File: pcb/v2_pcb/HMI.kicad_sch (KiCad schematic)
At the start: 34 parts, among them SW1101 BUTTON 1, SW1102 BUTTON 2, SW1103 BUTTON 3, U1100 SN74AHCT1G125DCKR, U1101 SN74AHCT1G125DCKR

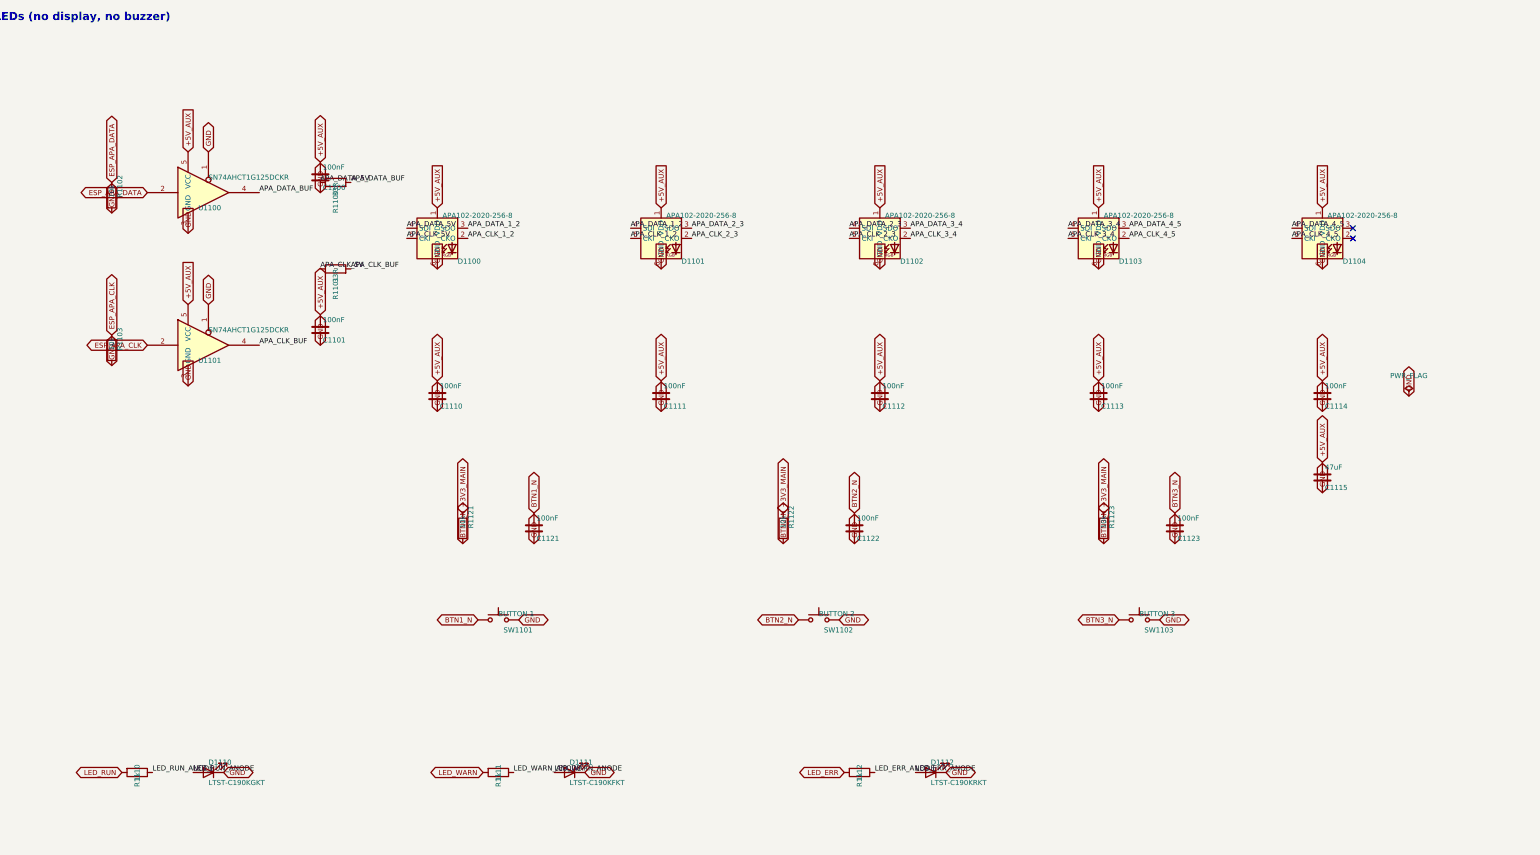
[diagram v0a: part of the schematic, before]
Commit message: switch mosfets
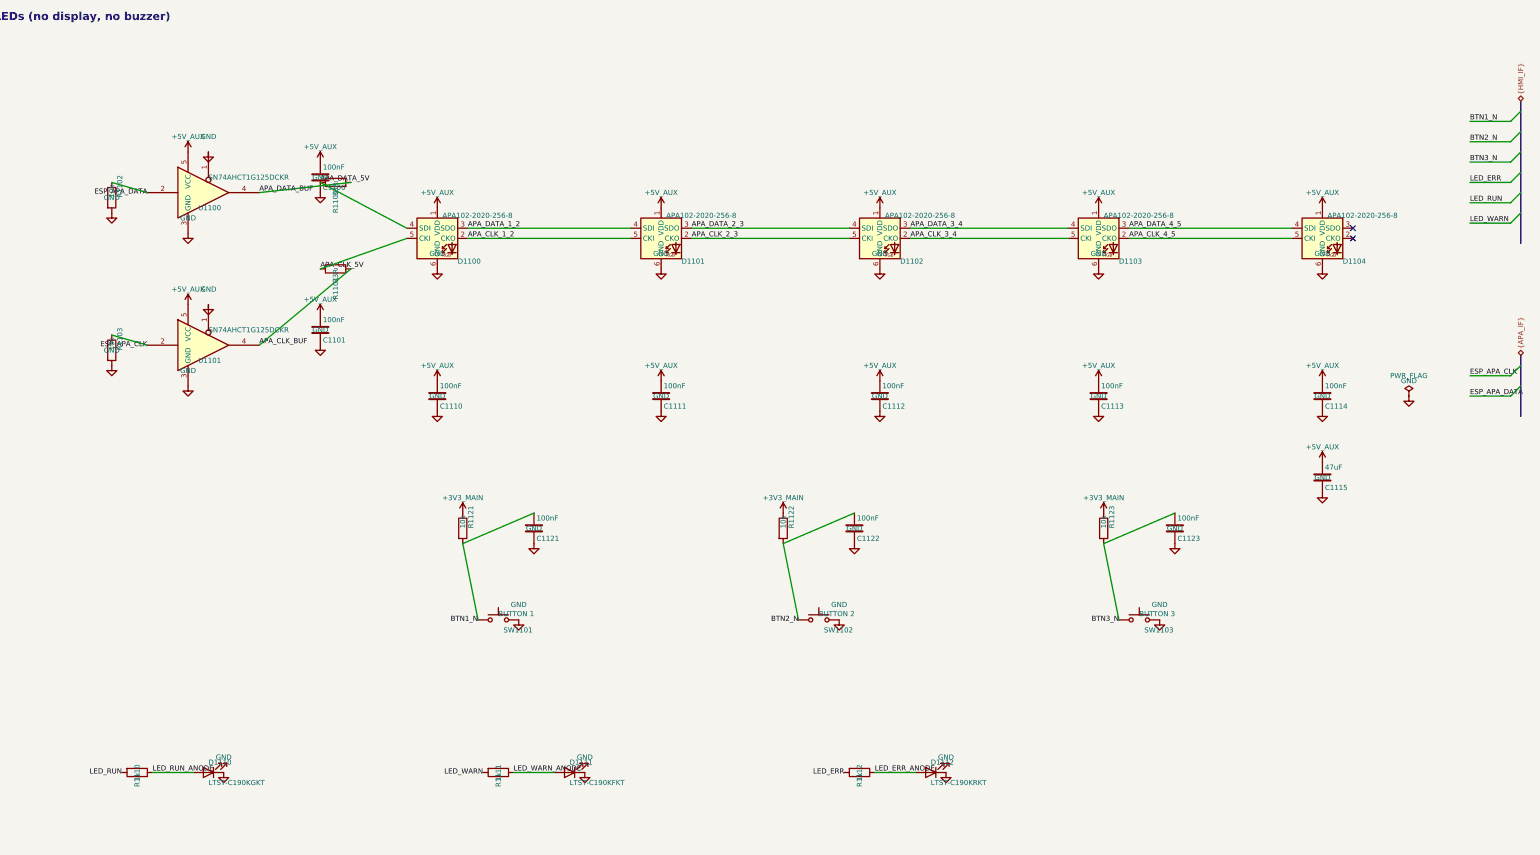
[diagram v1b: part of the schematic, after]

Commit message: minor fixes
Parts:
- C1100, C1101, C1110, C1111, C1112, C1113, C1114, C1121, C1122, C1123: value 100nF -> 100nF 50V X7R; Dielectric (none) -> X7R; MPN (none) -> CGA2B3X7R1H104K050BE; Manufacturer (none) -> TDK; Qualification (none) -> AEC-Q200; Termination (none) -> Soft termination; Tolerance (none) -> ±10%; Voltage (none) -> 50 VDC
- C1115: value 47uF -> 47uF 10V X7R; footprint Capacitor_SMD:C_0805_2012Metric -> Capacitor_SMD:C_1210_3225Metric; Dielectric (none) -> X7R; MPN (none) -> C1210X476K8RACAUTO; Manufacturer (none) -> KEMET (Yageo Group); Qualification (none) -> AEC-Q200; Release_Status (none) -> Verify effective capacitance under worst-case DC bias; Termination (none) -> FT-CAP flexible termination; Tolerance (none) -> ±10%; Voltage (none) -> 10 VDC
- D1100, D1101, D1102, D1103, D1104: Design_Note (none) -> Include the five LEDs in the +5V_AUX worst-case current and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; Manufacturer APA Electronic -> iPixel LED Light Co., Ltd.
- D1110: value LTST-C190KGKT -> ASMT-RF45-AN002 YELLOW GREEN; Color (none) -> Yellow green; Current (none) -> 20 mA maximum; visual-qualify at fitted 1 kΩ drive; MPN LTST-C190KGKT -> ASMT-RF45-AN002; Manufacturer Lite-On -> Broadcom; Operating_Temperature (none) -> -40 to +100 °C; Qualification (none) -> Automotive qualified
- D1111: value LTST-C190KFKT -> ASMT-RJ45-AQ502 ORANGE; Color (none) -> Orange; Current (none) -> 20 mA maximum; visual-qualify at fitted 1 kΩ drive; MPN LTST-C190KFKT -> ASMT-RJ45-AQ502; Manufacturer Lite-On -> Broadcom; Operating_Temperature (none) -> -40 to +100 °C; Qualification (none) -> Automotive qualified
- D1112: value LTST-C190KRKT -> ASMT-RR45-AQ902 RED; Color (none) -> Red; Current (none) -> 20 mA maximum; visual-qualify at fitted 1 kΩ drive; MPN LTST-C190KRKT -> ASMT-RR45-AQ902; Manufacturer Lite-On -> Broadcom; Operating_Temperature (none) -> -40 to +100 °C; Qualification (none) -> Automotive qualified
- R1100, R1101: MPN (none) -> CRCW040233R0FKED; Manufacturer (none) -> Vishay; Power (none) -> 0.063 W; TCR (none) -> ±100 ppm/K; Tolerance (none) -> ±1%
- R1102, R1103, R1121, R1122, R1123: MPN (none) -> CRCW040210K0FKED; Manufacturer (none) -> Vishay; Power (none) -> 0.063 W; TCR (none) -> ±100 ppm/K; Tolerance (none) -> ±1%
- R1110, R1111, R1112: MPN (none) -> CRCW04021K00FKED; Manufacturer (none) -> Vishay; Power (none) -> 0.063 W; TCR (none) -> ±100 ppm/K; Tolerance (none) -> ±1%
- SW1101: value BUTTON 1 -> KMR223NG ULC LFG; Contact (none) -> Gold ULC; 1 µA minimum at 1.8 V; MPN KMR221GLFS -> Y78B22324FP; Manufacturer C&K -> Littelfuse (C&K); Operating_Temperature (none) -> -40 to +125 °C
- SW1102: value BUTTON 2 -> KMR223NG ULC LFG; Contact (none) -> Gold ULC; 1 µA minimum at 1.8 V; MPN KMR221GLFS -> Y78B22324FP; Manufacturer C&K -> Littelfuse (C&K); Operating_Temperature (none) -> -40 to +125 °C
- SW1103: value BUTTON 3 -> KMR223NG ULC LFG; Contact (none) -> Gold ULC; 1 µA minimum at 1.8 V; MPN KMR221GLFS -> Y78B22324FP; Manufacturer C&K -> Littelfuse (C&K); Operating_Temperature (none) -> -40 to +125 °C
